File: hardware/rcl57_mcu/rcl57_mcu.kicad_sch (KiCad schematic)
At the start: 25 parts, among them J1 TMC1500 p1-13, J2 TMC1500 p28-16, J3 STLINK, Q1 DMP2240UDM-7, Q2 DMP2240UDM-7, Q3 DMP2240UDM-7, Q4 DMP2240UDM-7, U1 STM32F103TBUx, U2 TLC5929PWP, U3 TLV70033_SOT23-5, U4 11AA080/TT

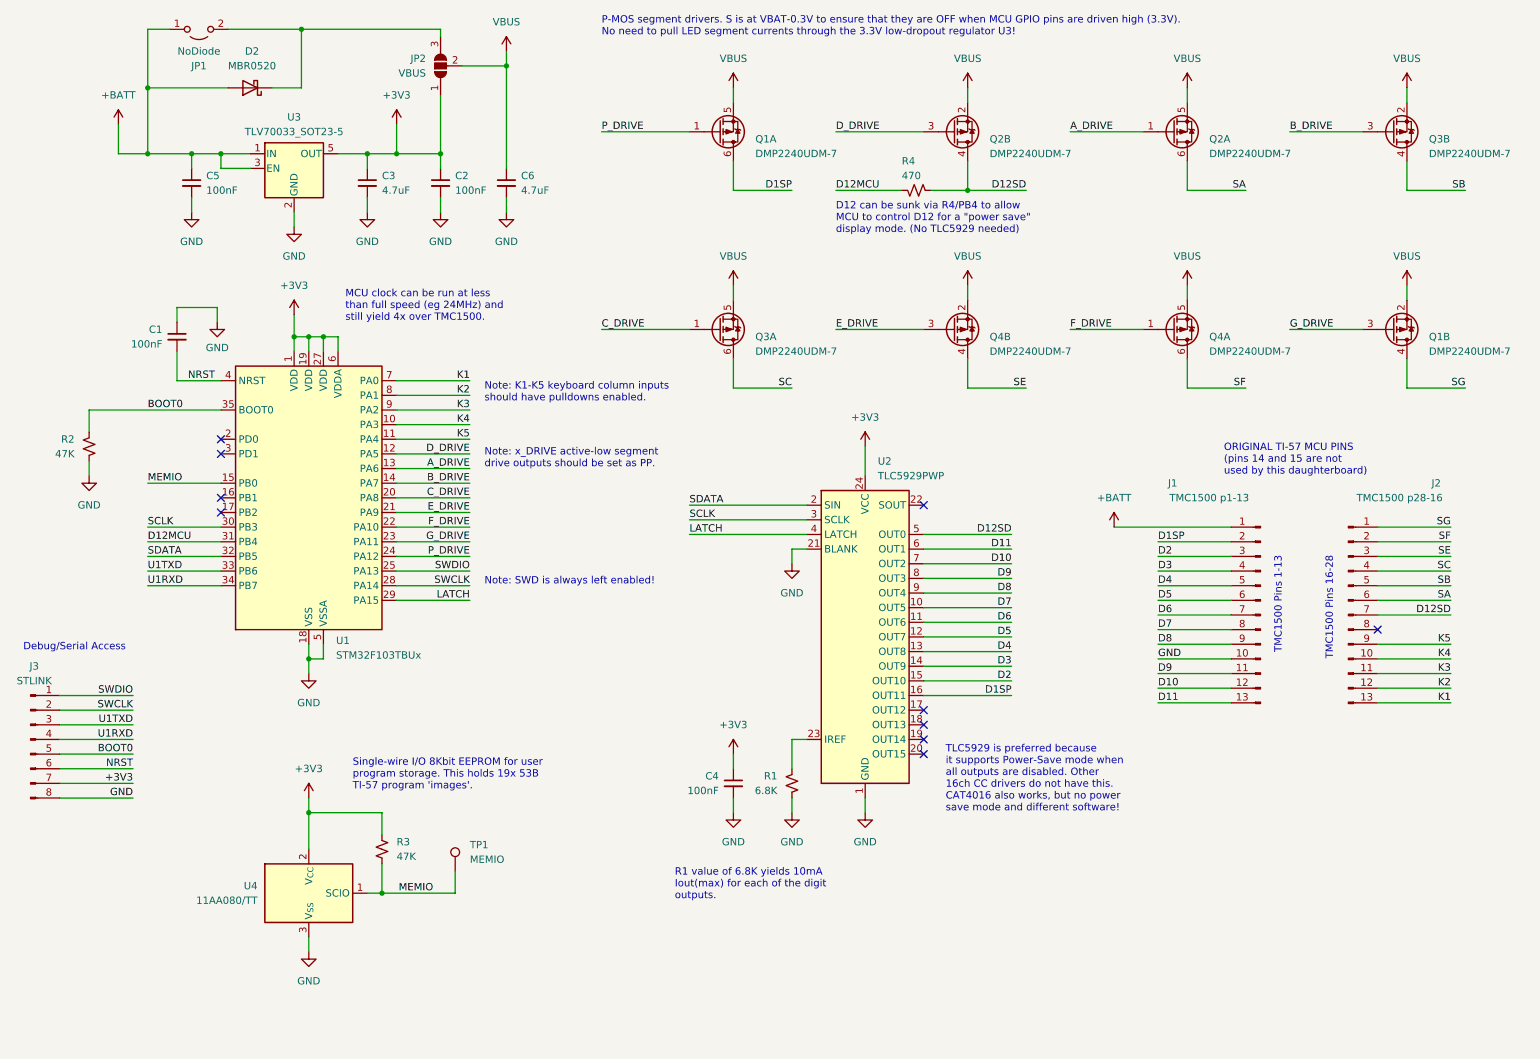
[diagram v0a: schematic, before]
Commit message: working on TI55 donor board
ADC key column read, UNIO EEPROM read/init, power-save mode. Assumes V2 PCB with 2K pulldowns on K1-K5 inputs.

Updated schematic and PCB to "v3" to include the pulldown pack and simplify power options. V3 board not yet sent out for fabrication.
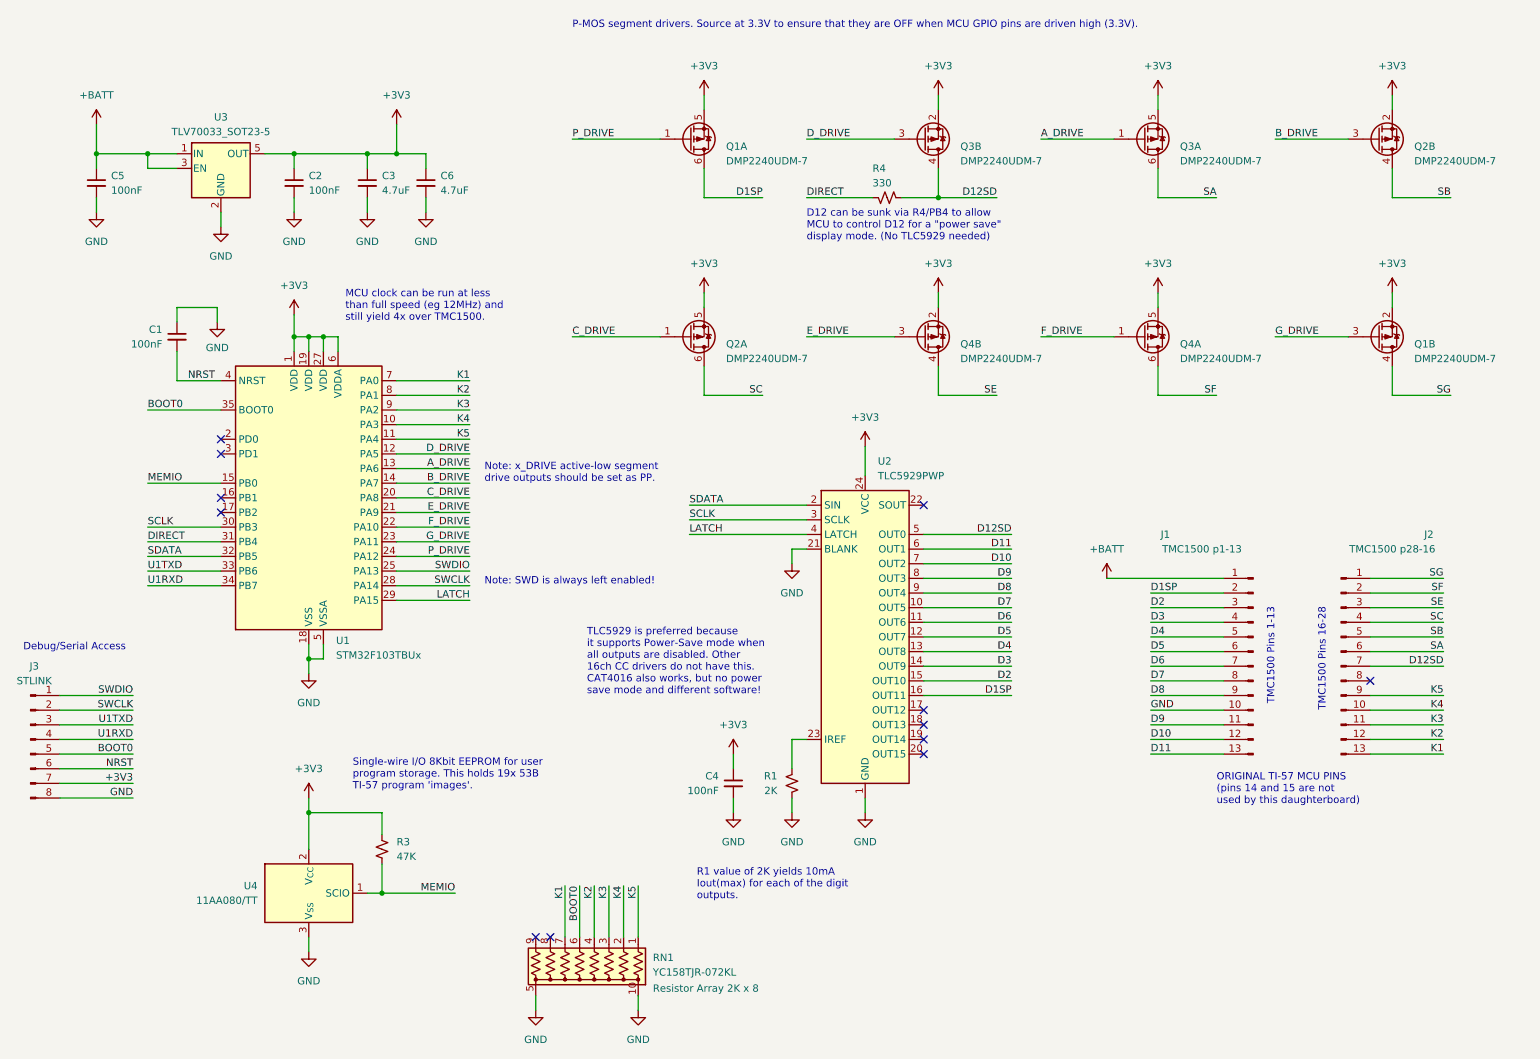
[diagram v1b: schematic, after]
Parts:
- removed D2: MBR0520, Diode_SMD:D_SOD-123, symbol Diode:MBR0520
- removed JP1: NoDiode, Jumper:SolderJumper-2_P1.3mm_Open_RoundedPad1.0x1.5mm, symbol Jumper:Jumper_2_Open
- removed JP2: VBUS, Jumper:SolderJumper-3_P1.3mm_Open_RoundedPad1.0x1.5mm_NumberLabels, symbol Jumper:SolderJumper_3_Open
- removed R2: 47K, Resistor_SMD:R_0805_2012Metric_Pad1.20x1.40mm_HandSolder, symbol Device:R_Small_US
- removed TP1: MEMIO, TestPoint:TestPoint_Pad_D1.5mm, symbol Connector:TestPoint
- added RN1: YC158TJR-072KL, Resistor_SMD:R_Array_Convex_5x0603, symbol ti57_library:R_Network_YC158T
- R1: value 6.8K -> 2K
- R4: value 470 -> 330
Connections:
- net VBUS is gone; now on net +3V3: C6.1, Q1.2 (SB), Q1.5 (SA), Q2.2 (SB), Q2.5 (SA), Q3.2 (SB), Q3.5 (SA), Q4.2 (SB), Q4.5 (SA)
- net A_DRIVE: now also Q3.1 (GA); no longer Q2.1 (GA)
- net BOOT0: now also RN1.6 (R5)
- net B_DRIVE: now also Q2.3 (GB); no longer Q3.3 (GB)
- net C_DRIVE: now also Q2.1 (GA); no longer Q3.1 (GA)
- net D12SD: now also Q3.4 (DB); no longer Q2.4 (DB)
- net D_DRIVE: now also Q3.3 (GB); no longer Q2.3 (GB)
- net GND: now also RN1.10 (common2), RN1.5 (common1)
- net K1: now also RN1.7 (R6)
- net K2: now also RN1.4 (R4)
- net K3: now also RN1.3 (R3)
- net K4: now also RN1.2 (R2)
- net K5: now also RN1.1 (R1)
- net SA: now also Q3.6 (DA); no longer Q2.6 (DA)
- net SB: now also Q2.4 (DB); no longer Q3.4 (DB)
- net SC: now also Q2.6 (DA); no longer Q3.6 (DA)
- net D12MCU renamed DIRECT
- no-connect marks 10 -> 12
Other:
- note added: "MCU clock can be run at less than full speed (eg 12MHz) and still yield 4x over TMC1500."
- note added: "P-MOS segment drivers. Source at 3.3V to ensure that they are OFF when MCU GPIO pins are driven high (3.3V)."
- note added: "R1 value of 2K yields 10mA Iout(max) for each of the digit outputs."
- note removed: "MCU clock can be run at less than full speed (eg 24MHz) and still yield 4x over TMC1500."
- note removed: "Note: K1-K5 keyboard column inputs should have pulldowns enabled."
- note removed: "P-MOS segment drivers. S is at VBAT-0.3V to ensure that they are OFF when MCU GPIO pins are driven high (3.3V). No need to pull LED segment currents through the 3.3V low-dropout regulator U3!"
- note removed: "R1 value of 6.8K yields 10mA Iout(max) for each of the digit outputs."
- moved on the sheet: C2, C5, C6, J1, J2, U3
